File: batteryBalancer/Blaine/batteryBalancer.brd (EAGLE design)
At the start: 101.6 x 101.6 mm, 36 parts

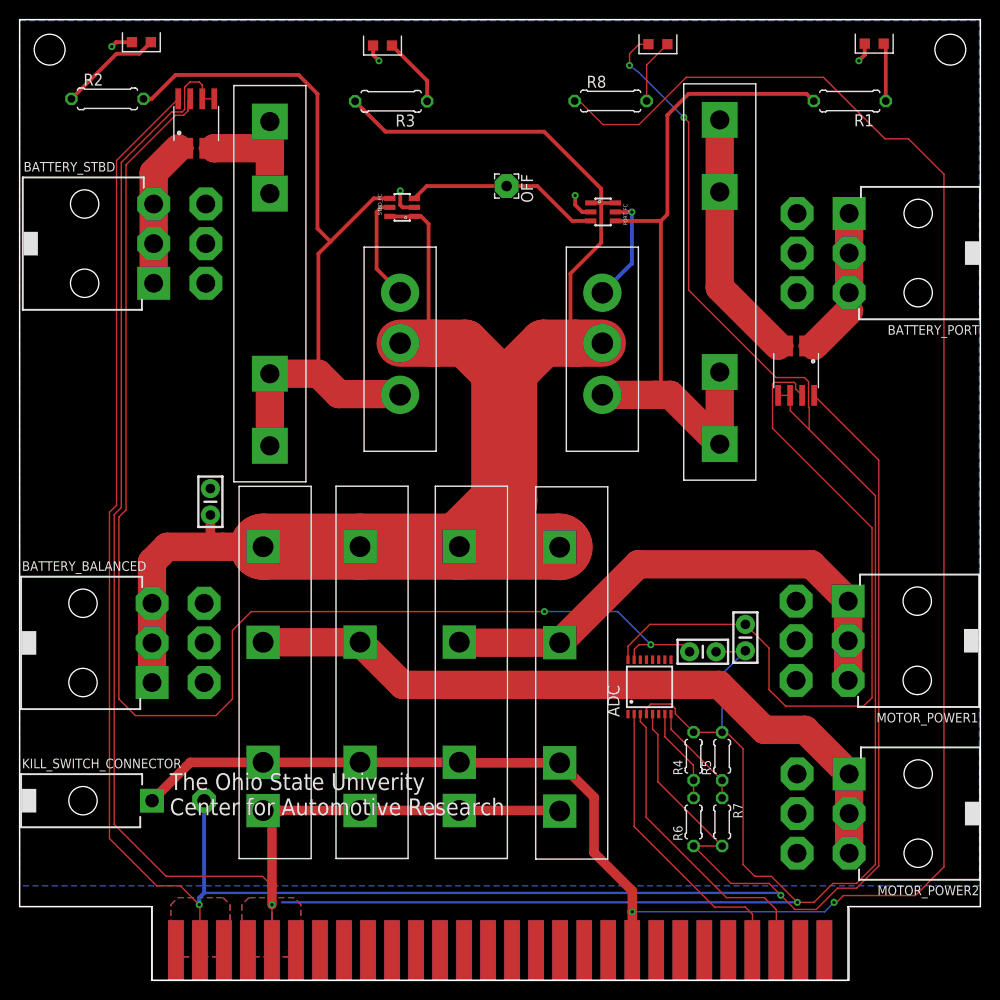
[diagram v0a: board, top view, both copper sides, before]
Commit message: Added testpoints
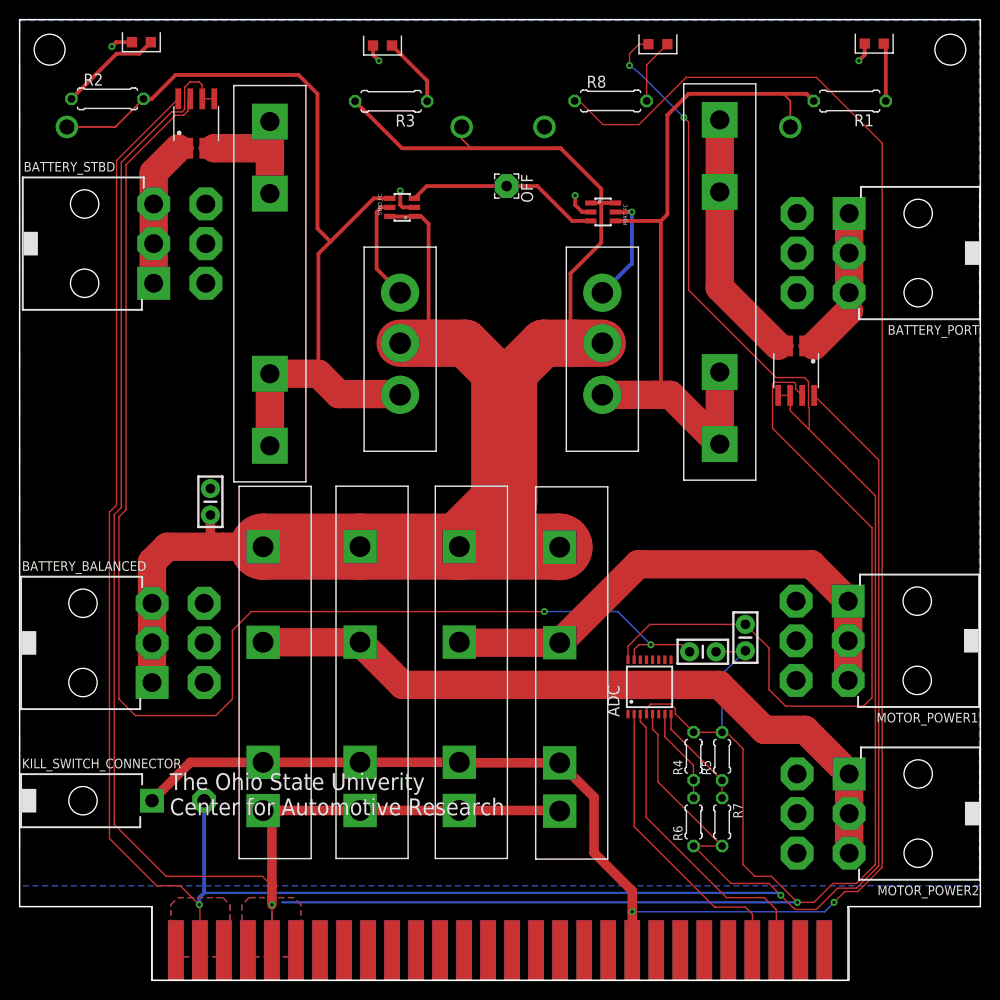
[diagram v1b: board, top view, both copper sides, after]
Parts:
- added U$1, U$2, U$3, U$4: 5010_C, 5010_c:5010_C
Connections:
- net BALANCED_POWER: now also U$3.P$1
- net GND: now also U$4.P$1
- net PORT_SOURCE: now also U$2.P$1
- net STBD_UNBALANCED: now also U$1.P$1
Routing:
- net KILL_SWITCH: track 222.4 -> 211.6 mm
- net STBD_UNBALANCED: track 81.5 -> 90.8 mm
- net PORT_SOURCE: track 75.3 -> 79.1 mm
- net BALANCED_POWER: track 176.0 -> 178.7 mm
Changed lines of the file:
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@@
 <layer number="14" name="Route14" color="1" fill="6" visible="no" active="no"/>
 <layer number="15" name="Route15" color="4" fill="6" visible="no" active="no"/>
-<layer number="16" name="Bottom" color="1" fill="1" visible="yes" active="yes"/>
+<layer number="16" name="Bottom" color="1" fill="1" visible="no" active="yes"/>
 <layer number="17" name="Pads" color="2" fill="1" visible="yes" active="yes"/>
 <layer number="18" name="Vias" color="2" fill="1" visible="yes" active="yes"/>
@@
 <layer number="59" name="tCarbon" color="7" fill="1" visible="no" active="no"/>
 <layer number="60" name="bCarbon" color="7" fill="1" visible="no" active="no"/>
+<layer number="88" name="SimResults" color="9" fill="1" visible="no" active="no"/>
+<layer number="89" name="SimProbes" color="9" fill="1" visible="no" active="no"/>
 <layer number="90" name="Modules" color="5" fill="1" visible="no" active="no"/>
 <layer number="91" name="Nets" color="2" fill="1" visible="no" active="no"/>
@@
 <attribute name="PROD_ID" value="CAP-08370" x="76.75" y="36.25" size="1.778" layer="27" rot="R270" display="off"/>
 </element>
+<element name="U$1" library="5010_c" package="5010_C" value="5010_C" x="5" y="90.25"/>
+<element name="U$2" library="5010_c" package="5010_C" value="5010_C" x="81.5" y="90.25"/>
+<element name="U$3" library="5010_c" package="5010_C" value="5010_C" x="46.75" y="90.25"/>
+<element name="U$4" library="5010_c" package="5010_C" value="5010_C" x="55.5" y="90.25"/>
 </elements>
 <signals>
@@
 <wire x1="89.375" y1="99.0625" x2="89.375" y2="97.875" width="0.4064" layer="1"/>
 <wire x1="89.375" y1="97.875" x2="88.75" y2="97.25" width="0.4064" layer="1"/>
+<contactref element="U$4" pad="P$1"/>
 </signal>
 <signal name="STBD_GATE">
@@
 <wire x1="31.5" y1="93.75" x2="31.5" y2="79.5" width="0.4064" layer="1"/>
 <wire x1="31.5" y1="79.5" x2="32.875" y2="78.125" width="0.4064" layer="1"/>
+<contactref element="U$1" pad="P$1"/>
+<wire x1="5" y1="90.25" x2="10.1225" y2="90.25" width="0.2" layer="1"/>
+<wire x1="10.1225" y1="90.25" x2="13.0975" y2="93.225" width="0.2" layer="1"/>
 </signal>
 <signal name="SCL">
@@
 <wire x1="58.25" y1="74.75" x2="58.25" y2="67.8825" width="0.4064" layer="1"/>
 <wire x1="58.25" y1="67.8825" x2="58.75" y2="67.3825" width="0.4064" layer="1"/>
-<wire x1="38.69" y1="89.75" x2="55.4626" y2="89.75" width="0.4064" layer="1"/>
-<wire x1="35.4775" y1="92.9625" x2="38.69" y2="89.75" width="0.4064" layer="1"/>
-<wire x1="55.4626" y1="89.75" x2="61.5" y2="83.7126" width="0.4064" layer="1"/>
 <wire x1="61.5" y1="83.7126" x2="61.5" y2="82.2125" width="0.4064" layer="1"/>
+<contactref element="U$3" pad="P$1"/>
+<wire x1="57.2126" y1="88" x2="61.5" y2="83.7126" width="0.4064" layer="1"/>
+<wire x1="35.4775" y1="92.9625" x2="40.44" y2="88" width="0.4064" layer="1"/>
+<wire x1="47.75" y1="88" x2="40.44" y2="88" width="0.4064" layer="1"/>
+<wire x1="47.75" y1="88" x2="57.2126" y2="88" width="0.4064" layer="1"/>
+<wire x1="46.75" y1="90.25" x2="46.75" y2="89" width="0.2" layer="1"/>
+<wire x1="46.75" y1="89" x2="47.75" y2="88" width="0.2" layer="1"/>
 </signal>
 <signal name="MOTOR_POWER1">
@@
 <contactref element="KILL_SWITCH_CONNECTOR" pad="1"/>
 <contactref element="R8" pad="1"/>
-<wire x1="94" y1="89" x2="91.5" y2="89" width="0.1524" layer="1"/>
-<wire x1="91.5" y1="89" x2="85" y2="95.5" width="0.1524" layer="1"/>
-<wire x1="85" y1="95.5" x2="70.5" y2="95.5" width="0.1524" layer="1"/>
+<wire x1="84.25" y1="95.5" x2="70.5" y2="95.5" width="0.1524" layer="1"/>
 <wire x1="70.5" y1="95.5" x2="65.5" y2="90.5" width="0.1524" layer="1"/>
 <wire x1="61.69" y1="90.5" x2="65.5" y2="90.5" width="0.1524" layer="1"/>
@@
 <wire x1="85.1296" y1="7.25" x2="86.1296" y2="8.25" width="0.1524" layer="16"/>
 <via x="86.1296" y="8.25" extent="1-16" drill="0.35"/>
-<wire x1="94.7184" y1="8.9684" x2="97.75" y2="12" width="0.1524" layer="1"/>
-<wire x1="87.11603125" y1="8.9684" x2="94.7184" y2="8.9684" width="0.1524" layer="1"/>
-<wire x1="86.1296" y1="8.25" x2="86.39763125" y2="8.25" width="0.1524" layer="1"/>
-<wire x1="86.39763125" y1="8.25" x2="87.11603125" y2="8.9684" width="0.1524" layer="1"/>
+<wire x1="86.39763125" y1="8.25" x2="86.1296" y2="8.25" width="0.1524" layer="1"/>
 <via x="64.7855" y="7.25" extent="1-16" drill="0.35"/>
 <wire x1="64.7855" y1="7.25" x2="85.1296" y2="7.25" width="0.1524" layer="16"/>
-<wire x1="97.75" y1="12" x2="97.75" y2="85.25" width="0.1524" layer="1"/>
-<wire x1="97.75" y1="85.25" x2="94" y2="89" width="0.1524" layer="1"/>
+<wire x1="86.1296" y1="8.25" x2="87.2722" y2="9.3926" width="0.1524" layer="1"/>
+<wire x1="87.2722" y1="9.3926" x2="88.6534875" y2="9.3926" width="0.1524" layer="1"/>
+<wire x1="88.6534875" y1="9.3926" x2="91.2148" y2="11.9539125" width="0.1524" layer="1"/>
+<wire x1="91.2148" y1="88.5352" x2="84.25" y2="95.5" width="0.1524" layer="1"/>
+<wire x1="91.2148" y1="11.9539125" x2="91.2148" y2="88.5352" width="0.1524" layer="1"/>
 </signal>
 <signal name="OFF">
@@
 <wire x1="68.5" y1="81" x2="68.5" y2="91.5" width="0.4064" layer="1"/>
 <wire x1="68.5" y1="91.5" x2="70.75" y2="93.75" width="0.4064" layer="1"/>
-<wire x1="70.75" y1="93.75" x2="83.215" y2="93.75" width="0.4064" layer="1"/>
+<wire x1="80.75" y1="93.75" x2="70.75" y2="93.75" width="0.4064" layer="1"/>
+<wire x1="80.75" y1="93.75" x2="83.215" y2="93.75" width="0.4064" layer="1"/>
 <wire x1="83.215" y1="93.75" x2="83.9775" y2="92.9875" width="0.4064" layer="1"/>
+<contactref element="U$2" pad="P$1"/>
+<wire x1="81.5" y1="90.25" x2="81.5" y2="93" width="0.2" layer="1"/>
+<wire x1="81.5" y1="93" x2="80.75" y2="93.75" width="0.2" layer="1"/>
 </signal>
 <signal name="N$3">

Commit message: Done, made gerbers, time for lunch
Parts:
- removed KILL_SWITCH_CONNECTOR: 39-30-02?, con-molex-mini-fit:39-30-?02?
- added KILL_SWITCH: 39-30-02?, con-molex-mini-fit:39-30-?02?
- moved C3 9.08 mm to (68.1, 39.0), turned to 90 degrees
- moved MOTOR_POWER2 0.41 mm to (87.4, 17.9)
- moved BATTERY_PORT 0.32 mm to (87.4, 76.9)
- moved MOTOR_POWER1 0.22 mm to (87.4, 35.9)
- moved BATTERY_BALANCED 0.17 mm to (14.2, 35.7)
- turned OFF to 0 degrees
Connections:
- net 3.3V: now also KILL_SWITCH.2; no longer KILL_SWITCH_CONNECTOR.2
- net KILL_SWITCH: now also KILL_SWITCH.1; no longer KILL_SWITCH_CONNECTOR.1
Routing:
- net GND: track 12.3 -> 19.5 mm
- net LOGIC_GND: track 373.3 -> 376.6 mm
- net 3.3V: track 267.7 -> 265.5 mm
- net KILL_SWITCH: track 211.6 -> 212.2 mm
- net STBD_CURRENT: track 141.8 -> 141.2 mm
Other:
- board text added: "A0"
- board text added: "A1"
- board text added: "Address Resistors"
- board text added: "Balanced Power"
- board text added: "High"
- board text added: "Kill Switch"
- board text added: "Low"
- board text added: "Port Power"
- board text added: "Star Power"

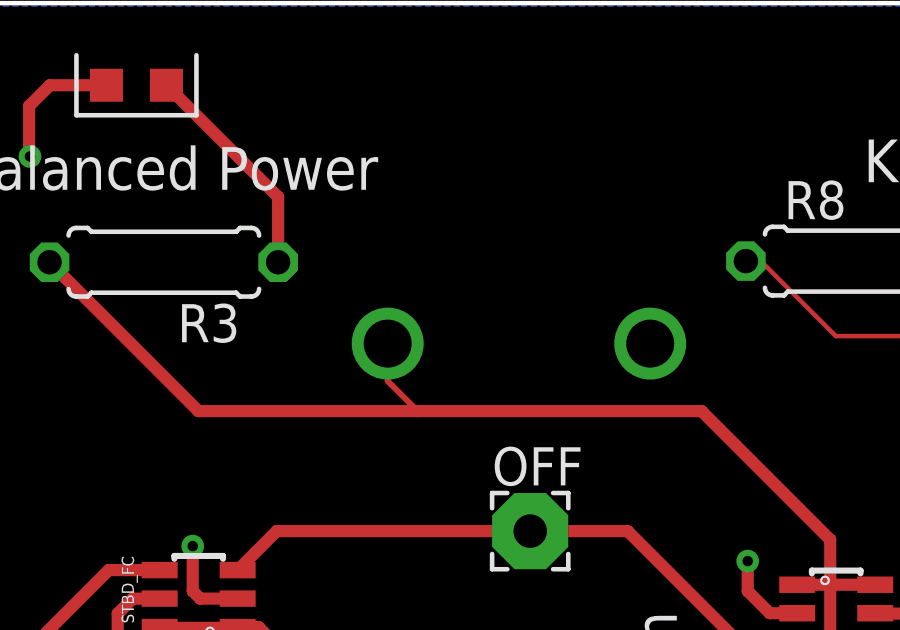
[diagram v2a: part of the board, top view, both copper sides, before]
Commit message: Got the gerber and also labeled the gnd test point
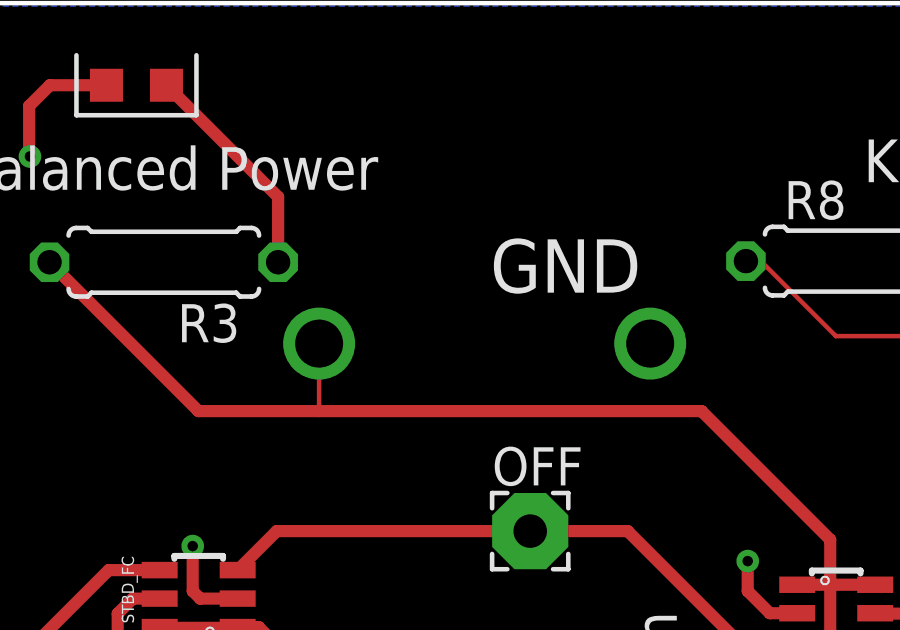
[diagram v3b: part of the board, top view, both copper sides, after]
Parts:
- moved U$3 2.29 mm to (44.5, 90.2)
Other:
- board text added: "GND"
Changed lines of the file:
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@@
 <text x="83.693" y="95.377" size="1.4224" layer="21">Port Power</text>
 <text x="9.398" y="95.885" size="1.4224" layer="21">Star Power</text>
+<text x="50.165" y="91.948" size="1.778" layer="21">GND</text>
 </plain>
 <attributes>
@@
 <element name="U$1" library="5010_c" package="5010_C" value="5010_C" x="5" y="90.25"/>
 <element name="U$2" library="5010_c" package="5010_C" value="5010_C" x="81.5" y="90.25"/>
-<element name="U$3" library="5010_c" package="5010_C" value="5010_C" x="46.75" y="90.25" smashed="yes"/>
+<element name="U$3" library="5010_c" package="5010_C" value="5010_C" x="44.464" y="90.25" smashed="yes"/>
 <element name="U$4" library="5010_c" package="5010_C" value="5010_C" x="55.5" y="90.25"/>
 <element name="KILL_SWITCH" library="con-molex-mini-fit" package="39-30-?02?" value="39-30-02?" x="14.1732" y="18.161" smashed="yes" rot="R270">
@@
 <wire x1="57.2126" y1="88" x2="61.5" y2="83.7126" width="0.4064" layer="1"/>
 <wire x1="35.4775" y1="92.9625" x2="40.44" y2="88" width="0.4064" layer="1"/>
-<wire x1="47.75" y1="88" x2="40.44" y2="88" width="0.4064" layer="1"/>
-<wire x1="47.75" y1="88" x2="57.2126" y2="88" width="0.4064" layer="1"/>
-<wire x1="46.75" y1="90.25" x2="46.75" y2="89" width="0.2" layer="1"/>
-<wire x1="46.75" y1="89" x2="47.75" y2="88" width="0.2" layer="1"/>
+<wire x1="44.45" y1="88" x2="40.44" y2="88" width="0.4064" layer="1"/>
+<wire x1="44.45" y1="88" x2="57.2126" y2="88" width="0.4064" layer="1"/>
 <wire x1="14.097" y1="39.9547" x2="14.1732" y2="39.8785" width="3" layer="1"/>
 <wire x1="15.605" y1="45.855" x2="14.097" y2="44.347" width="3" layer="1"/>
 <wire x1="14.097" y1="44.347" x2="14.097" y2="39.9547" width="3" layer="1"/>
+<wire x1="44.464" y1="90.25" x2="44.464" y2="88.014" width="0.1524" layer="1"/>
+<wire x1="44.464" y1="88.014" x2="44.45" y2="88" width="0.1524" layer="1"/>
 </signal>
 <signal name="MOTOR_POWER1">
